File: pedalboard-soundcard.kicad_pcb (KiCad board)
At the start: 2 copper layers, 65 x 56 mm, 83 parts, among them J1 RPi_GPIO, J2 Conn_02x03_Odd_Even, J3 Conn_02x03_Odd_Even, J4 Audio_Jack, J5 Audio_Jack, U1 AT24CS01-STUM, U2 NCP163, U3 NCP163, U4 PCM1863DBT, U5 NCP163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

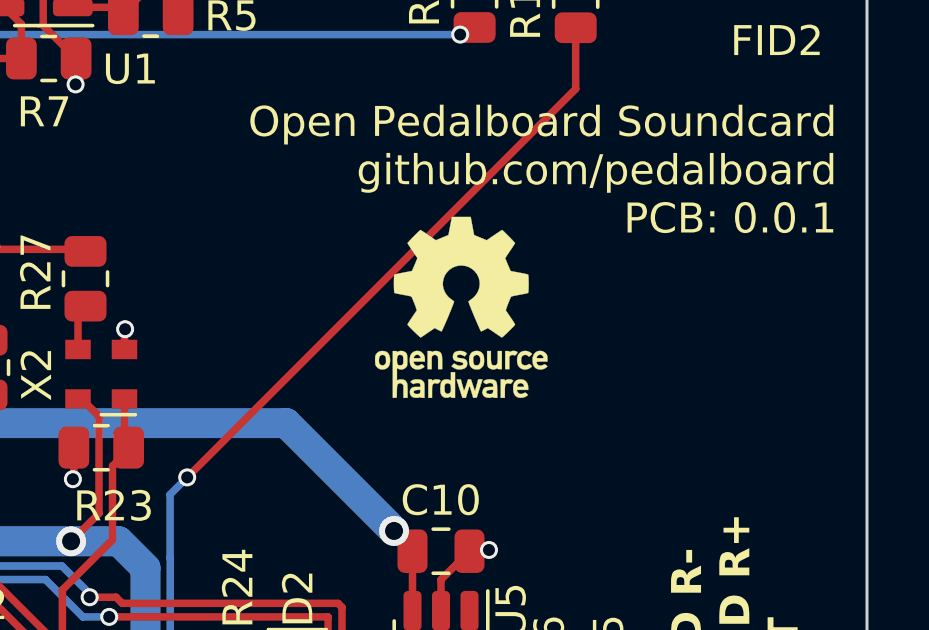
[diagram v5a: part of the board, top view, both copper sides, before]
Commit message: Add git commit to schema sheets and PCB sheet
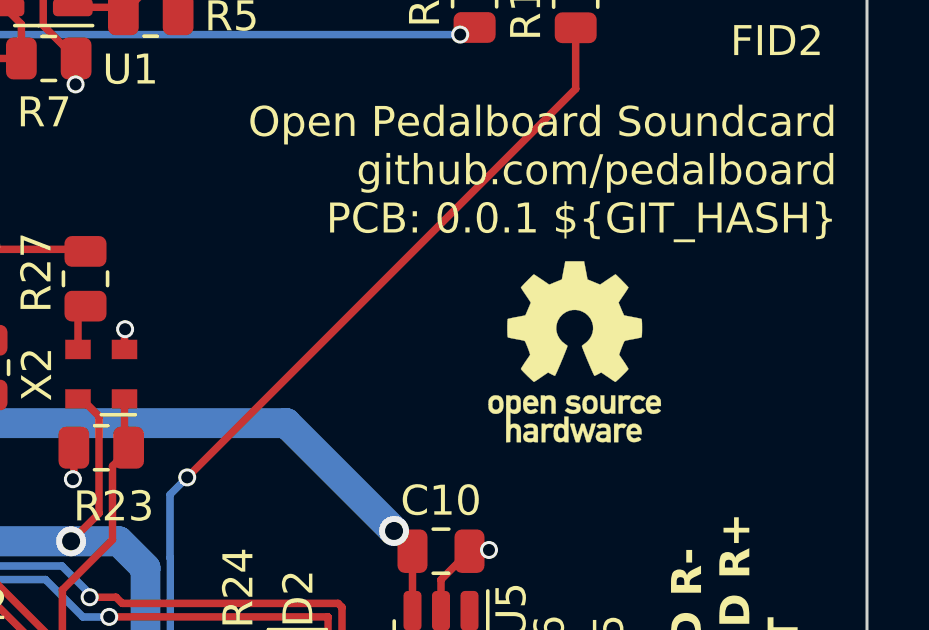
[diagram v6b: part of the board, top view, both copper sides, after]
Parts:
- moved SYM1 4.06 mm to (103.8, 73.3)
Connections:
- J4 pad RN: GND -> unconnected-(J4-PadRN)
- J4 pad TN: GND -> unconnected-(J4-PadTN)
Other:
- board text added: "${TITLE} ${COMPANY} PCB: ${REVISION} ${GIT_HASH}"
- board text removed: "${TITLE} ${COMPANY} PCB: ${REVISION}"
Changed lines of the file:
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@@
     (comment 1 "Source Code: https://github.com/pedalboard/pedalboard-hw")
     (comment 2 "License: CERN Open Hardware Licence Version 2 - Permissive")
+    (comment 3 "git hash: ${GIT_HASH}")
   )
   (layers
@@
   (net 92 "unconnected-(J5-PadRN)")
   (net 93 "unconnected-(J5-PadTN)")
+  (net 94 "unconnected-(J4-PadRN)")
+  (net 95 "unconnected-(J4-PadTN)")
   (footprint "pedalboard-soundcard:RPi_Hat_Mounting_Hole" locked (layer "F.Cu")
     (at 110 56)
@@
     (property "Sheetfile" "pedalboard-soundcard.kicad_sch")
     (property "Sheetname" "")
-    (property "Supplier" "https://www.digikey.com/en/products/detail/adafruit-industries-llc/2222/6238005")
+    (property "Supplier" "https://www.digikey.ch/en/products/detail/adafruit-industries-llc/2222/6238005")
     (attr through_hole)
     (fp_text reference "J1" (at -3.99 -22.62 180) (layer "F.SilkS")
@@
     (property "Sheetname" "ADC")
     (property "Supplier" "https://www.digikey.ch/de/products/detail/schurter-inc/4833-2320/2644235")
+    (property "dnp" "")
     (property "ki_description" "Audio Jack, 3 Poles (Stereo / TRS), Switched TR Poles (Normalling)")
     (property "ki_keywords" "audio jack receptacle stereo headphones phones TRS connector")
@@
       (net 5 "/ADC/inr+") (pintype "passive"))
     (pad "RN" thru_hole oval (at -2.5 -5) (size 1.6 2.3) (drill oval 0.8 1.5) (layers "*.Cu" "*.Mask")
-      (net 2 "GND") (pintype "passive"))
+      (net 94 "unconnected-(J4-PadRN)") (pintype "passive"))
     (pad "S" thru_hole oval (at 0 0) (size 2.2 1.2) (drill oval 1.4 0.4) (layers "*.Cu" "*.Mask")
       (net 2 "GND") (pintype "passive"))
@@
       (net 27 "/ADC/inl+") (pintype "passive"))
     (pad "TN" thru_hole oval (at 2.5 -5 180) (size 1.6 2.5) (drill oval 0.8 1.5) (layers "*.Cu" "*.Mask")
-      (net 2 "GND") (pintype "passive"))
+      (net 95 "unconnected-(J4-PadTN)") (pintype "passive"))
     (model "${KICAD7_3DMODEL_DIR}/Connector_Audio.3dshapes/Jack_3.5mm_CUI_SJ1-3525N_Horizontal.wrl"
       (offset (xyz 0 0 0))
@@
   )
   (footprint "Symbol:OSHW-Logo_5.7x6mm_SilkScreen" (layer "F.Cu")
-    (at 99.97 71.87)
+    (at 103.75 73.35)
     (descr "Open Source Hardware Logo")
     (tags "Logo OSHW")
@@
     (property "Sheetname" "DAC")
     (property "Supplier" "https://www.digikey.ch/de/products/detail/schurter-inc/4833-2320/2644235")
+    (property "dnp" "")
     (property "ki_description" "Audio Jack, 3 Poles (Stereo / TRS), Switched TR Poles (Normalling)")
     (property "ki_keywords" "audio jack receptacle stereo headphones phones TRS connector")
@@
     (effects (font (size 1 1) (thickness 0.2) bold) (justify left bottom))
   )
-  (gr_text "${TITLE}\n${COMPANY}\nPCB: ${REVISION}" (at 112.5 69.5) (layer "F.SilkS")
+  (gr_text "${TITLE}\n${COMPANY}\nPCB: ${REVISION} ${GIT_HASH}" (at 112.5 69.5) (layer "F.SilkS")
     (effects (font (size 1 1) (thickness 0.15)) (justify right bottom))
   )
